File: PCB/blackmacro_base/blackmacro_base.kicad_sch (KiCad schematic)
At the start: 171 parts, among them J1 MOD Power, J2 MOD I/O, J3 Dial_PowerConn, J4 Dial_MagEncoderConn, J5 Dial_MotorControlConn, J6 USB_C_Receptacle_USB2.0_16P, Q1 AO3415, Q2 AO3415, Q3 AO3415, SW1 SW_SPDT, U1 HTP4056-42-ESOP8, U2 74HC238, U3 SN74LVC1T45DBV, U4 BQ27427, U5 MT3608L

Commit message: 7-2-fab1, archive before switching to 8-2-fab1 (changed via diameters for cheaper tier, next change is changing bga diameter to 0.25 so i can use hasl)
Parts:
- U4: footprint Package_BGA:Texas_DSBGA-9_1.62x1.58mm_Layout3x3_P0.5mm -> footprints:Texas_DSBGA-9_1.62x1.58mm_Layout3x3_P0.5mm
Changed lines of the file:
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@@
 			)
 		)
-		(property "Footprint" "Package_BGA:Texas_DSBGA-9_1.62x1.58mm_Layout3x3_P0.5mm"
+		(property "Footprint" "footprints:Texas_DSBGA-9_1.62x1.58mm_Layout3x3_P0.5mm"
 			(at 215.9 78.74 0)
 			(hide yes)

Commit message: 10-2-fab1 the production version. project files have already been updated to 11-2-fab2, with critical fixes with the logic shifter (incorrect schematics in 10-2-fab1).
this commit is mostly to archive the production files, please use 11-2-fab2.
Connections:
- net +3V3: now also U3.1 (VCCA), U3.5 (DIR)
- net +5V: now also U3.6 (VCCB)
- net GND: now also C4.2, C5.2
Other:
- note added: "IM A FUCKING IDIOT"

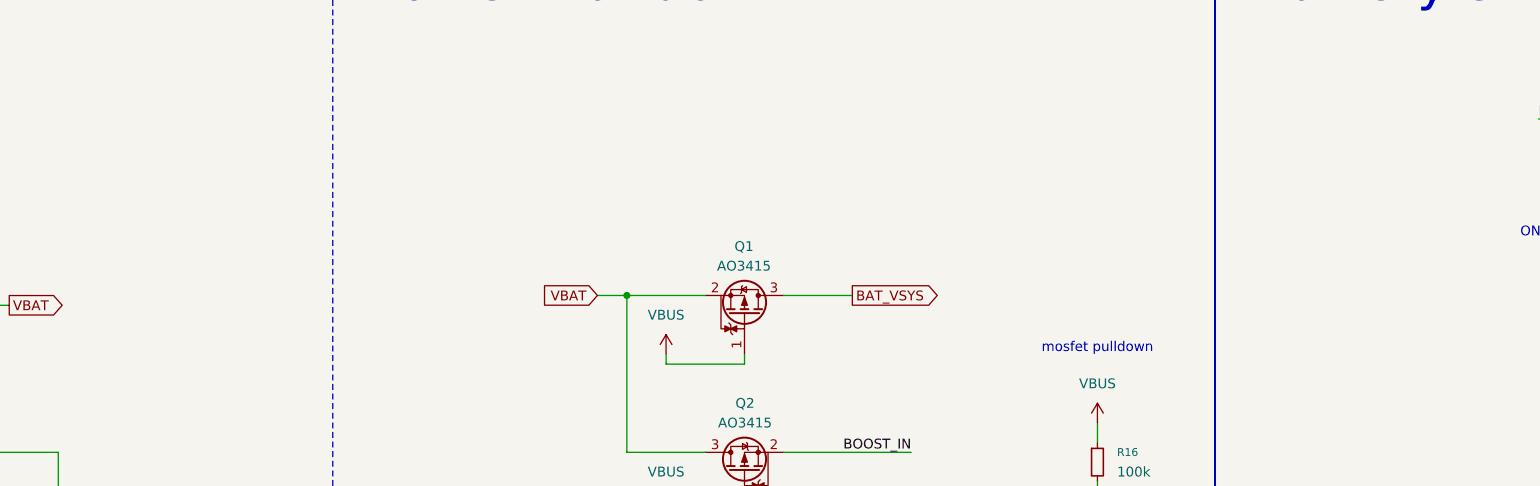
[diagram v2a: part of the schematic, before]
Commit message: V2 pre-release BOM not done, updating gitignore to remove keebio-parts
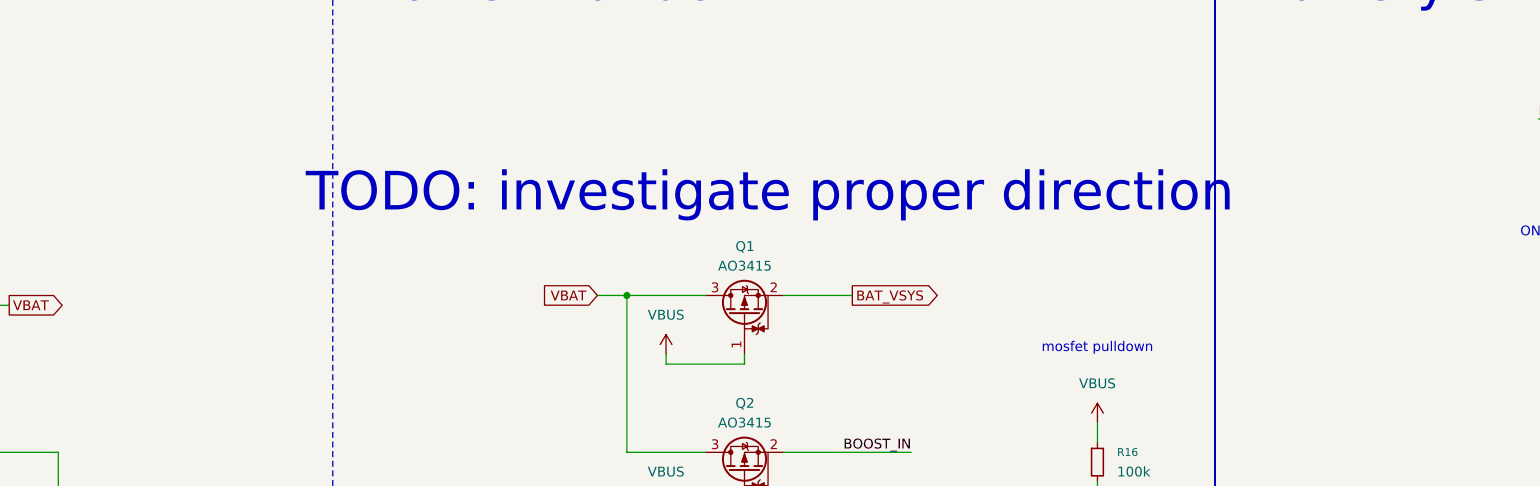
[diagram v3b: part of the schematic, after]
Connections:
- net BAT_VSYS: now also Q1.2 (S); no longer Q1.3 (D)
- net VBAT: now also Q1.3 (D); no longer Q1.2 (S)
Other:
- note added: "TODO: investigate proper direction"
- moved on the sheet: Q1
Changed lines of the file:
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@@
 		)
 	)
+	(text "TODO: investigate proper direction"
+		(exclude_from_sim no)
+		(at 355.092 46.482 0)
+		(effects
+			(font
+				(size 5 5)
+			)
+		)
+	)
 	(text "Defaults to 2.5A limit"
 		(exclude_from_sim no)
@@
 	(symbol
 		(lib_id "custom:AO3415")
-		(at 351.79 62.23 270)
-		(mirror x)
+		(at 351.79 62.23 90)
 		(unit 1)
 		(body_style 1)
@@
 		(dnp no)
 		(property "Reference" "Q1"
-			(at 351.7265 53.34 90)
+			(at 351.8535 53.34 90)
 			(show_name no)
 			(do_not_autoplace no)
@@
 		)
 		(property "Value" "AO3415"
-			(at 351.7265 55.88 90)
+			(at 351.8535 55.88 90)
 			(show_name no)
 			(do_not_autoplace no)
@@
 		)
 		(property "Footprint" "Package_TO_SOT_SMD:SOT-23_Handsoldering"
-			(at 349.885 57.15 0)
+			(at 353.695 57.15 0)
 			(hide yes)
 			(show_name no)
@@
 		)
 		(property "Datasheet" "https://item.szlcsc.com/192491.html"
-			(at 347.98 57.15 0)
+			(at 355.6 57.15 0)
 			(hide yes)
 			(show_name no)
@@
 		(in_pos_files yes)
 		(dnp no)
-		(fields_autoplaced yes)
 		(property "Reference" "Q2"
 			(at 351.8535 73.66 90)
